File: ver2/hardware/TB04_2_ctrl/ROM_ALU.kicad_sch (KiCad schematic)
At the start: 31 parts, among them IC601 74HC161N, J601 Conn_02x05_Odd_Even, SW601 SW_Coded_SH-7050, U601 74LS273, U602 74HC273, U603 28C256, U604 28C256, U605 74HC74, U606 74HC273, U607 74HC238

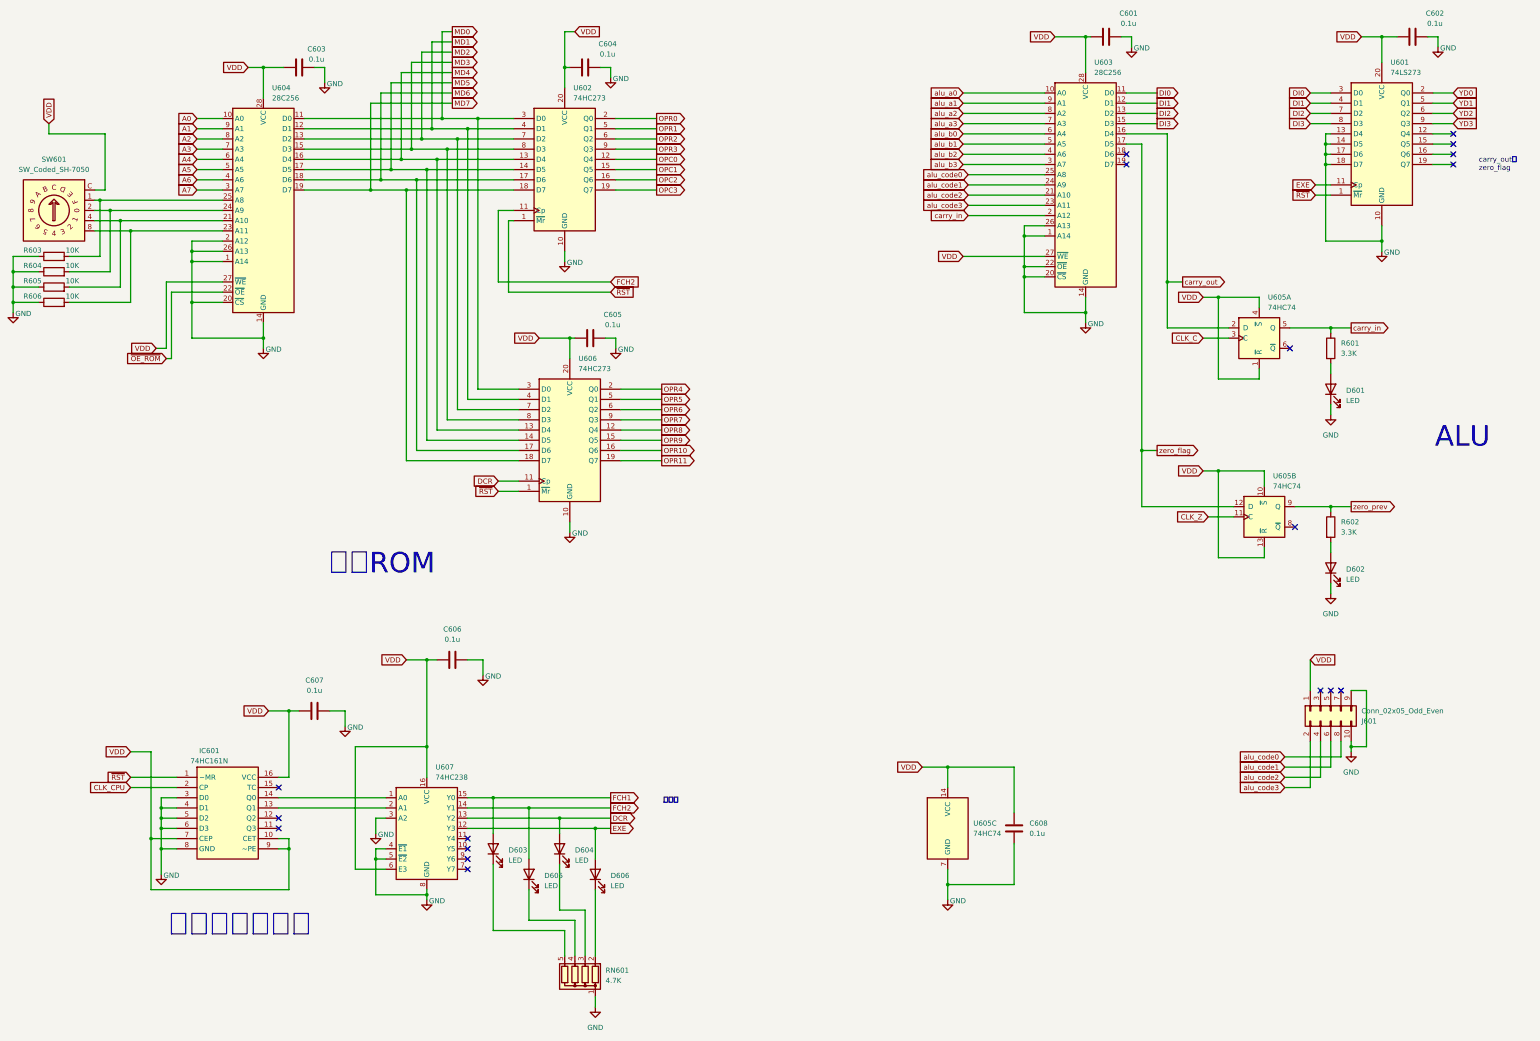
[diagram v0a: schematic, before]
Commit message: ver2: 制御基板を分割完了・不要シートを整理(基板4分割の3枚目)
TB04_2_ctrl を分割完了。ai-reviewで検証し合格。
- 64信号すべてバスへ引き出し済み、ピン位置は確定表と完全一致
- 署名が変わったのは J101 のみ(USB-C→40ピンバスヘッダ)
- 電源入口は TB04_4_io のみ。他基板はバス1のVDD/GNDから受ける
- 各プロジェクトから未使用シートのファイルを削除

Co-Authored-By: Claude Opus 5 <noreply@anthropic.com>
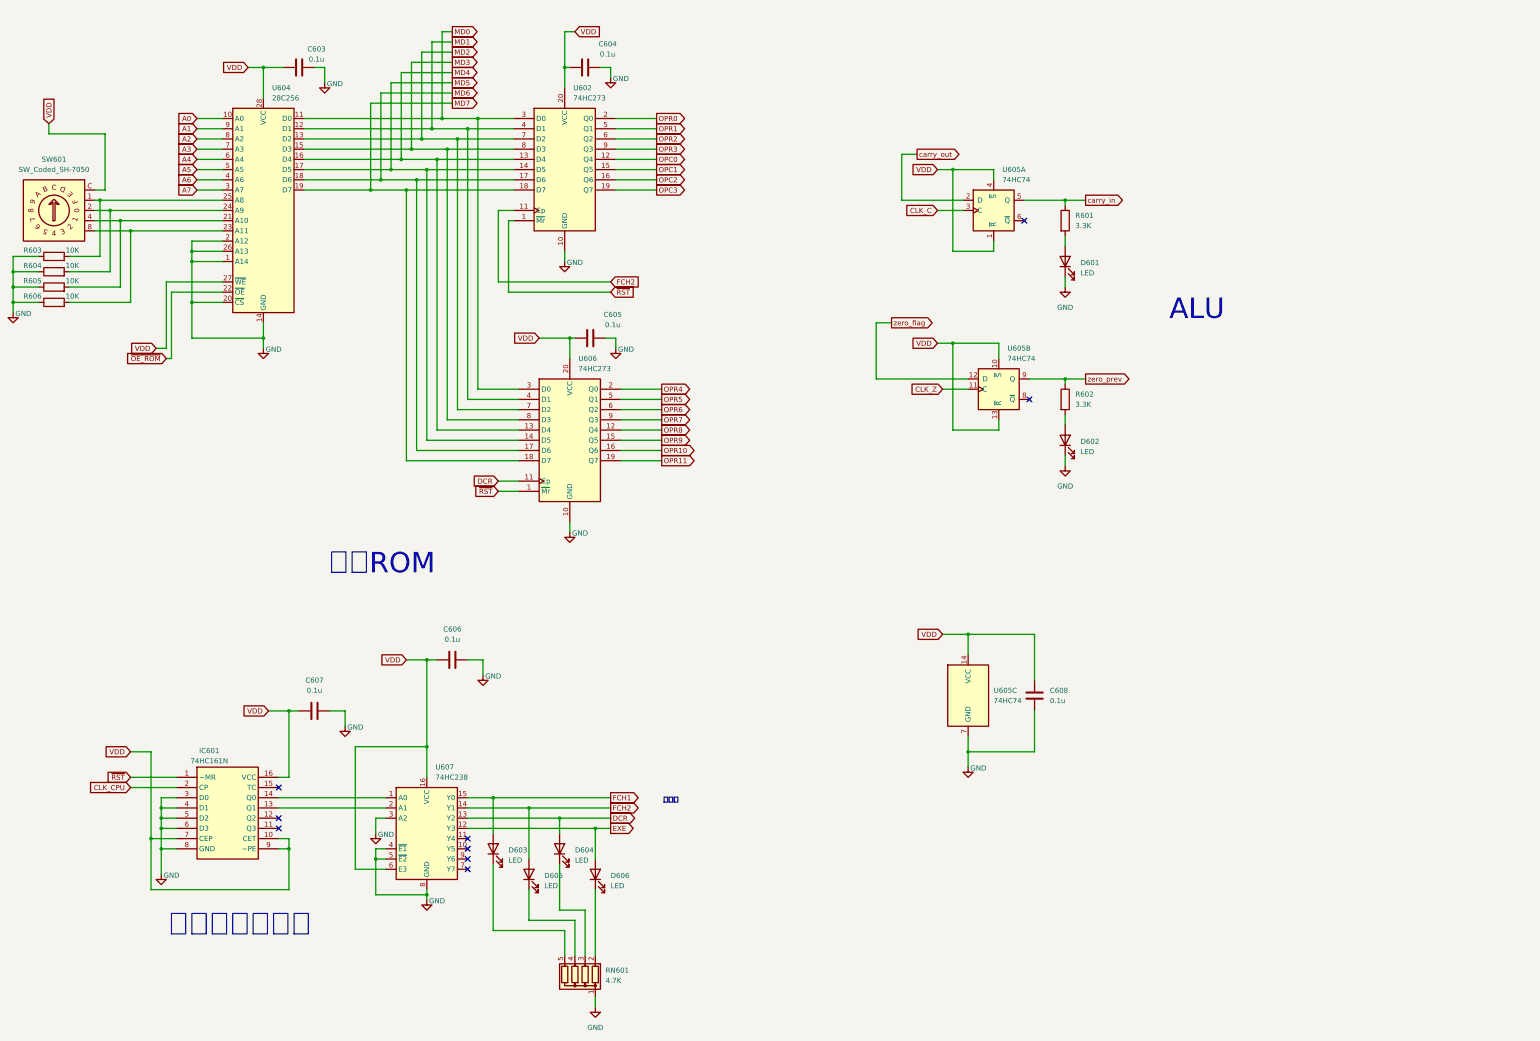
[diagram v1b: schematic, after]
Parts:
- removed C601, C602: 0.1u, Capacitor_THT:C_Disc_D4.3mm_W1.9mm_P5.00mm, symbol Device:C
- removed J601: Conn_02x05_Odd_Even, symbol Connector_Generic:Conn_02x05_Odd_Even
- removed U601: 74LS273, Package_DIP:DIP-20_W7.62mm_Socket, symbol 74xx:74LS273
- removed U603: 28C256, Package_DIP:DIP-28_W15.24mm_Socket, symbol Memory_EEPROM:28C256
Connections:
- no-connect marks 18 -> 9
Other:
- note removed: "carry_outと zero_flag"
- moved on the sheet: C608, D601, D602, R601, R602, U605A, U605B, U605C
